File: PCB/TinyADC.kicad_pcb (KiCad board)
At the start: 2 copper layers, 49.8 x 24.4 mm, 15 parts, among them J1 Conn_01x03, J2 Conn_01x05, J3 Conn_01x03, J4 Conn_01x03, J5 Conn_02x03_Odd_Even, U1 ATtiny85-20PU

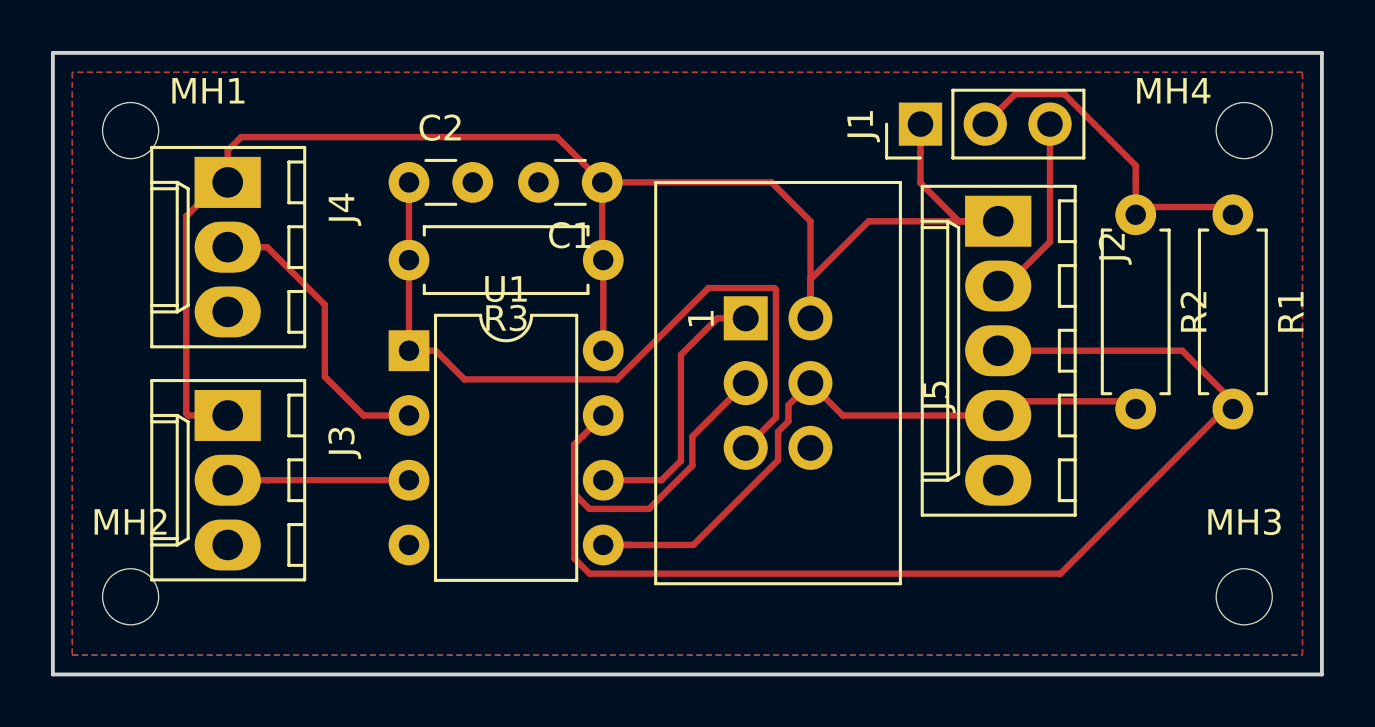
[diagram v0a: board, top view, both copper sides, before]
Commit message: position stecker geändert
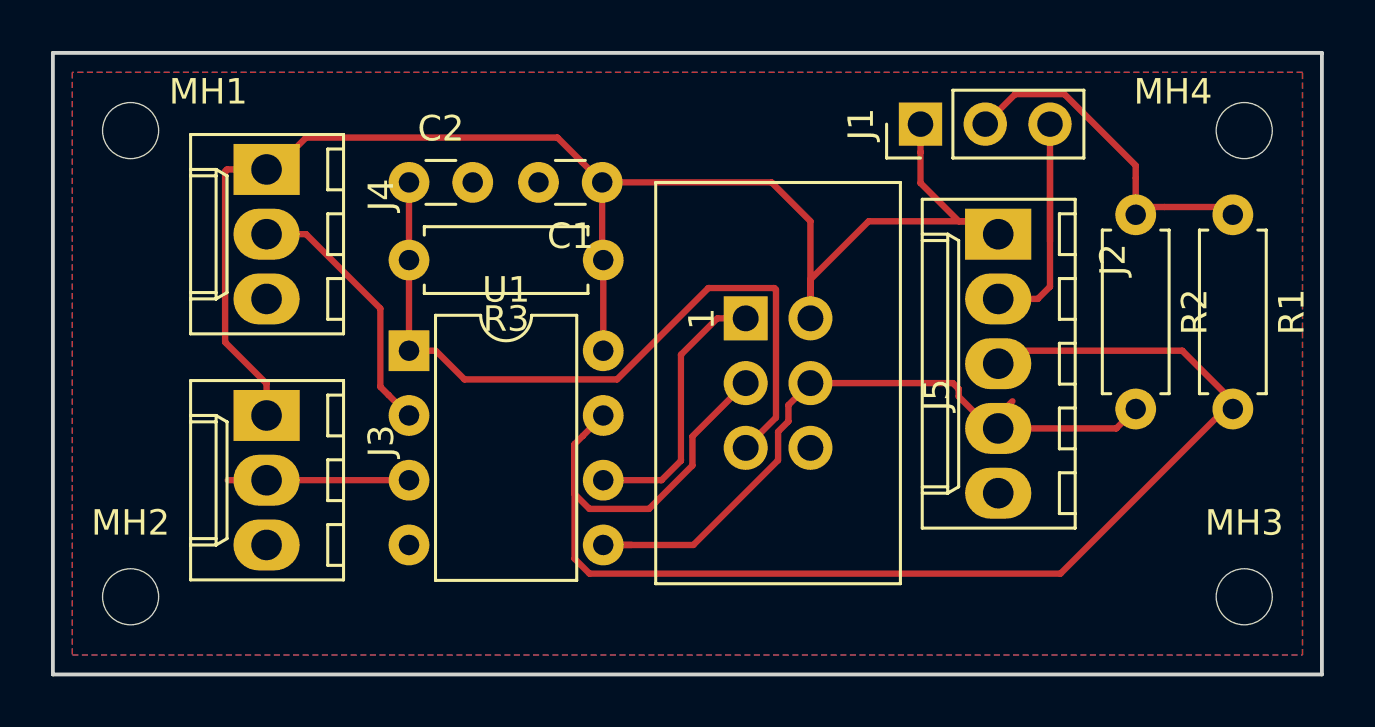
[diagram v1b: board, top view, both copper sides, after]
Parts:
- moved J4 1.61 mm to (124.5, 102.9)
- moved J3 1.52 mm to (124.5, 112.5)
- moved J2 0.51 mm to (153.2, 105.4)
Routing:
- net +3V3: track 7.37 -> 12.3 mm
- net VCC: track 63.5 -> 61.4 mm
- net /SDA: track 26.4 -> 27.7 mm
- net /ADC3: track 11.5 -> 10.3 mm
